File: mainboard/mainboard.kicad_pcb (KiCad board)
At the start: 4 copper layers, 68 x 86.5 mm, 74 parts, among them J1 Servo, J2 Buzzer, J4 Button Interface, J5 Power, J6 Release Button, J7 Extra Pins, Q1 BSS138, Q2 BSS138, Q3 BSS138, Q4 BSS138, Q5 BSS138, Q6 BSS138, SW1 SW_Push, U1 RP2040, U2 W25Q128JVS, U3 RV-3028-C7, U4 ITR9608-F, U5 TCA9535RTWR, U6 KW4-56NCWB-P-Y, Y1 Crystal_ABM8

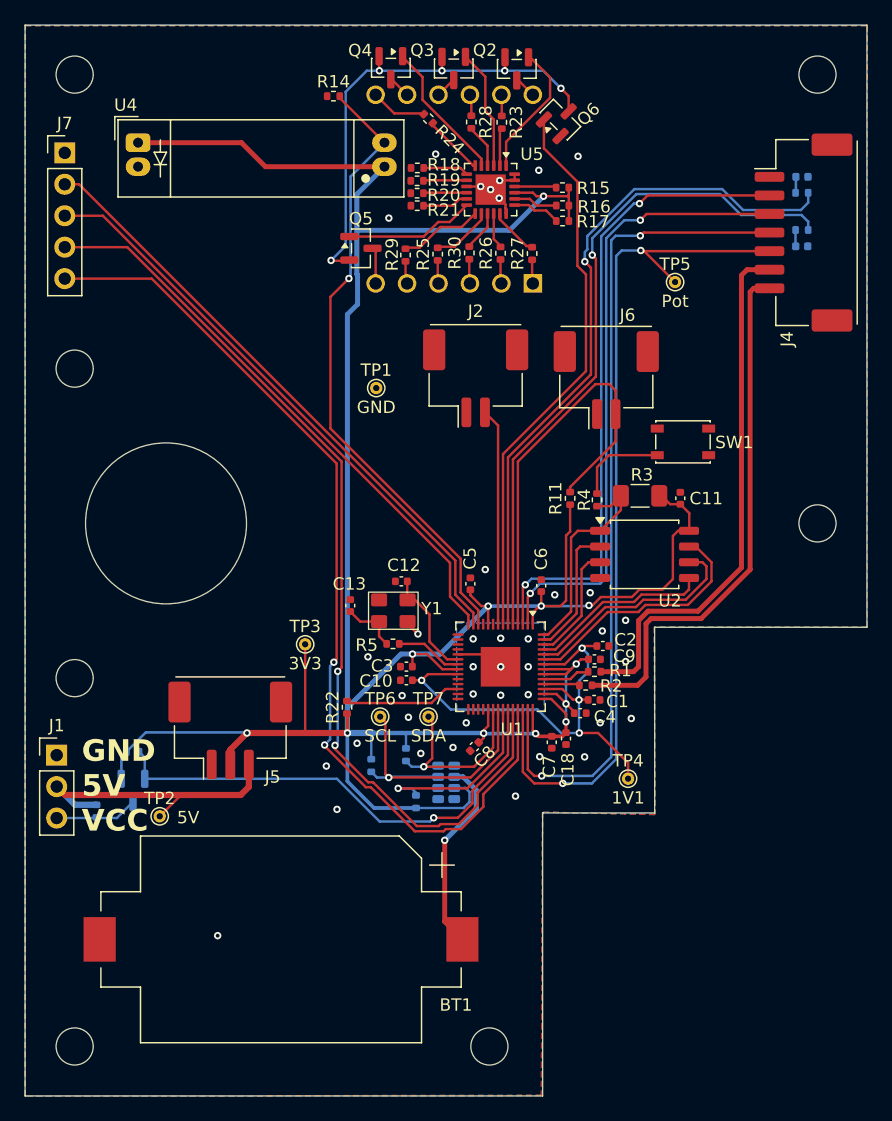
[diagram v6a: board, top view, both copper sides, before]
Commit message: added indicator LEDs
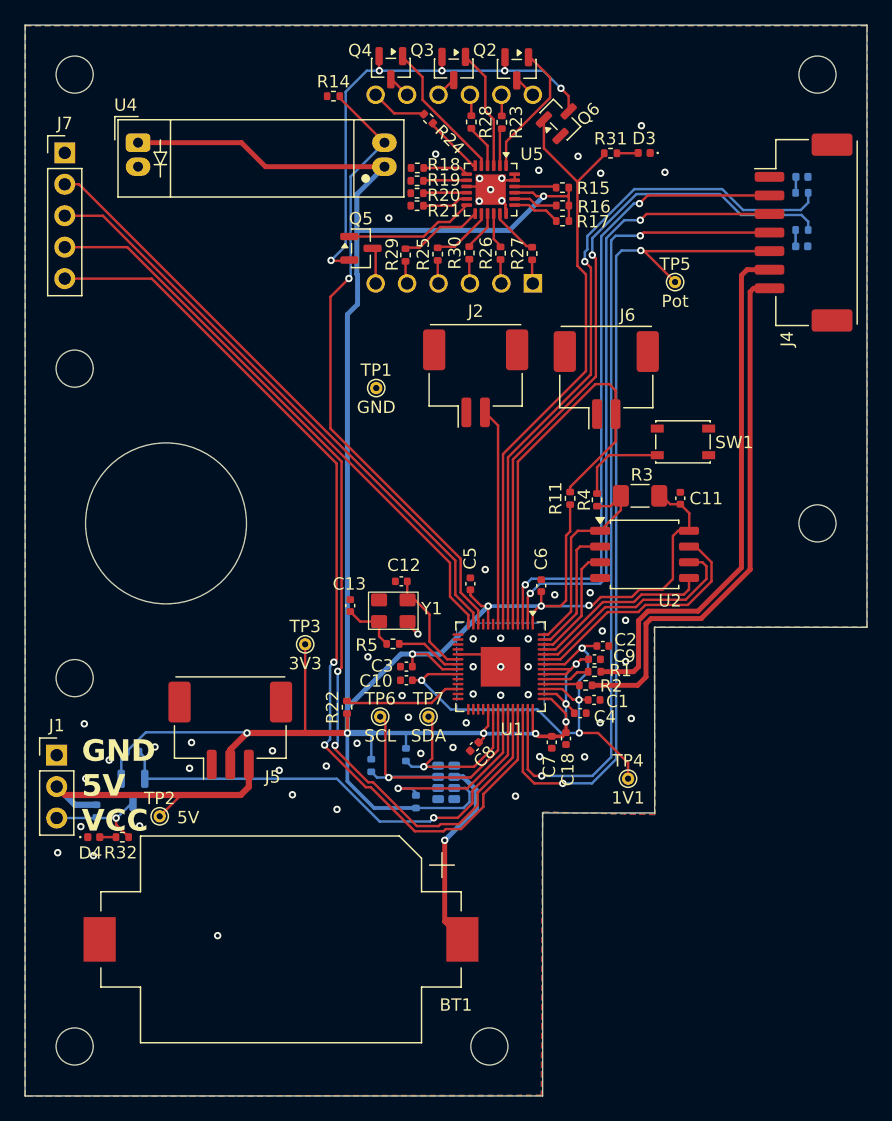
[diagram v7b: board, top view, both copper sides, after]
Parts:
- added D3: LED, LED_SMD:LED_0402_1005Metric, F.Cu at (127.8, 67.8)
- added D4: LED, LED_SMD:LED_0402_1005Metric, F.Cu at (83.3, 123.1)
- added R31: 220, Resistor_SMD:R_0402_1005Metric, F.Cu at (125.0, 67.8)
- added R32: 220, Resistor_SMD:R_0402_1005Metric, F.Cu at (85.6, 123.1)
- U6: value KW4-56NCWB-P-Y -> 11405
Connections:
- U5 pad 11: /7-Segment/CAL -> Net-(U5-P11)
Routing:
- net /7-SEG_PWM: track 45.0 -> 48.2 mm
- net GND: track 13.3 -> 10.9 mm, vias 39 -> 56
- net Net-(J1-Pin_3): track 6.70 -> 8.65 mm, vias 0 -> 1
- net Net-(D3-A): track 0.00 -> 1.73 mm
- net Net-(D4-A): track 0.00 -> 1.31 mm

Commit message: Minor fixes
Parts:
- removed R12: 10k, Resistor_SMD:R_0402_1005Metric
- added TP10: 7SEG VCC, TestPoint:TestPoint_THTPad_D1.0mm_Drill0.5mm, F.Cu at (127.8, 62.5)
- added TP8: SCL, TestPoint:TestPoint_THTPad_D1.0mm_Drill0.5mm, F.Cu at (135.0, 67.0)
- added TP9: SDA, TestPoint:TestPoint_THTPad_D1.0mm_Drill0.5mm, F.Cu at (131.8, 66.9)
- moved Q1 0.33 mm to (86.2, 119.5), turned to 180 degrees
- moved D4 0.10 mm to (83.3, 123.2)
- moved R32 0.10 mm to (85.6, 123.2)
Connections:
- Q1 pad 1: +3.3V -> /SERVO_PWM
- Q1 pad 2: /SERVO_PWM -> GND
- R13 pad 2: Net-(J1-Pin_3) -> unconnected-(R13-Pad2)
- R32 pad 2: Net-(J1-Pin_3) -> /SERVO_PWM
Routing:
- net /7-SEG_SCL: track 3.91 -> 21.6 mm, vias 0 -> 1
- net /7-SEG_SDA: track 3.59 -> 19.1 mm, vias 0 -> 1
- net +3.3V: track 251.1 -> 238.2 mm, vias 12 -> 11
- net /7-SEG_PWM: track 48.2 -> 54.9 mm
- net /SERVO_PWM: track 39.7 -> 43.1 mm, vias 1 -> 2
- net Net-(J1-Pin_3): track 8.65 -> 7.38 mm, vias 1 -> 0
